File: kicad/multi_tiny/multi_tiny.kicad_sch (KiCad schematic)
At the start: 55 parts, among them J1 Conn_02x03_Odd_Even, J2 Conn_01x08, J3 28pin ZIF, J4 Conn_01x17, SW1 SW_SPDT, SW2 SW_SPDT, SW4 SW_SPST, SW5 SW_SPST, U1 CD4052B, U2 CD4052B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

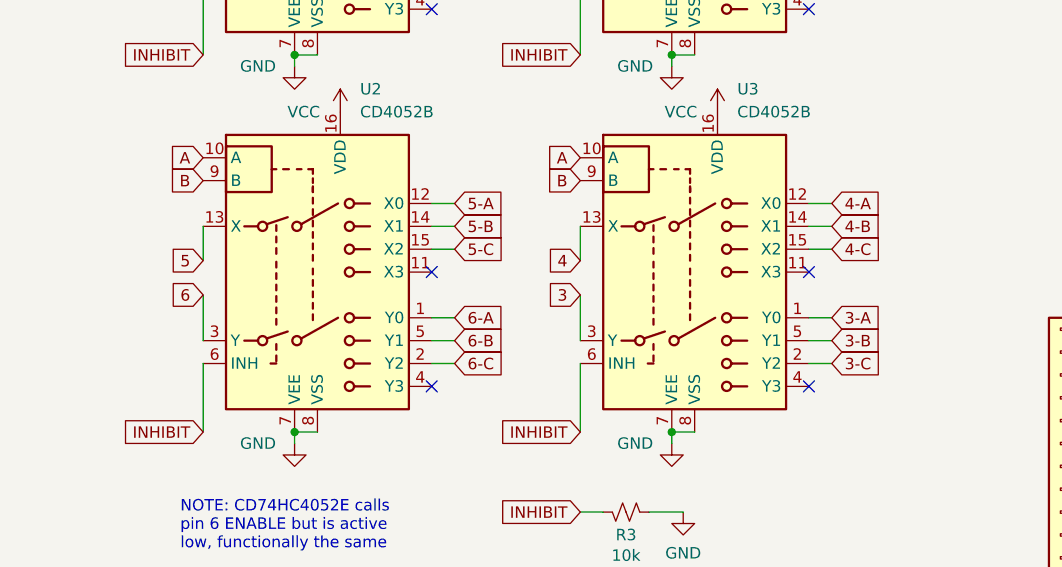
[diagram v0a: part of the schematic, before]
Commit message: Route PCB
And fix CD4052/target pins arrangement
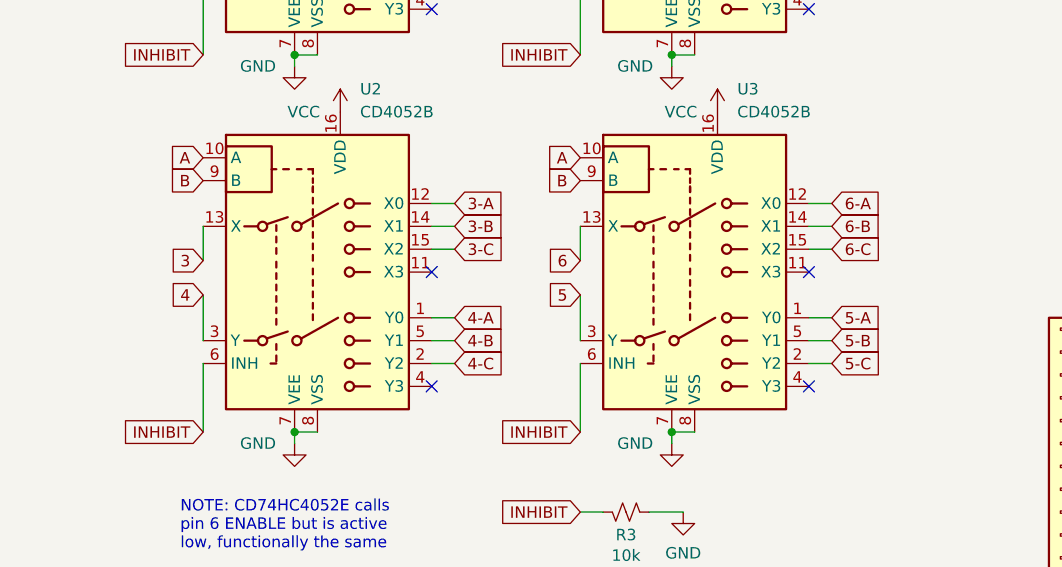
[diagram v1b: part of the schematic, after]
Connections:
- net 3: now also U2.13 (X); no longer U3.3 (Y)
- net 3-A: now also U2.12 (X0); no longer U3.1 (Y0)
- net 3-B: now also U2.14 (X1); no longer U3.5 (Y1)
- net 3-C: now also U2.15 (X2); no longer U3.2 (Y2)
- net 4-A: now also U2.1 (Y0); no longer U3.12 (X0)
- net 4-B: now also U2.5 (Y1); no longer U3.14 (X1)
- net 4-C: now also U2.2 (Y2); no longer U3.15 (X2)
- net 5: now also U3.3 (Y); no longer U2.13 (X)
- net 5-A: now also U3.1 (Y0); no longer U2.12 (X0)
- net 5-B: now also U3.5 (Y1); no longer U2.14 (X1)
- net 5-C: now also U3.2 (Y2); no longer U2.15 (X2)
- net 6: now also U3.13 (X); no longer U2.3 (Y)
- net 6-A: now also U3.12 (X0); no longer U2.1 (Y0)
- net 6-B: now also U3.14 (X1); no longer U2.5 (Y1)
- net 6-C: now also U3.15 (X2); no longer U2.2 (Y2)
- net GND: now also U2.3 (Y); no longer U3.13 (X)
